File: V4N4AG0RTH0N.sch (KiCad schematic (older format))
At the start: 24 parts, among them SW1 SW_Push, U1 ATmega32U4-A, Y1 16MHz

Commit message: Almost done?
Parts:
- removed USB1: Molex-0548190589, random-keyboard-parts:Molex-0548190589, symbol random-keyboard-parts:Molex-0548190589
- added D10, D11, D12, D13, D14, D15, D16, D17, D18, D19, D20, D21, D22, D23, D24, D25, D26, D27, D28, D29, D3, D30, D31, D32, D33, D34, D35, D36, D37, D38, D39, D4, D40, D41, D42, D43, D44, D45, D46, D47, D48, D49, D5, D50, D6, D9: SOD-123, Diode_SMD:D_SOD-123, symbol Device:D_Small
- added D51, D52, D53: LED, LED_THT:LED_D3.0mm, symbol Device:LED
- added F2: Polyfuse_Small, Fuse:Fuse_1206_3216Metric, symbol Device:Polyfuse_Small
- added MX10, MX11, MX12, MX13, MX14, MX15, MX16, MX17, MX18, MX19, MX20, MX21, MX22, MX23, MX24, MX25, MX26, MX27, MX28, MX29, MX3, MX30, MX31, MX32, MX33, MX34, MX35, MX36, MX37, MX38, MX39, MX4, MX40, MX41, MX42, MX43, MX44, MX45, MX48, MX49, MX5, MX50, MX6, MX9: MX-NoLED, MX_Alps_Hybrid:MX-1U-NoLED, symbol MX_Alps_Hybrid:MX-NoLED
- added MX46, MX47: MX-NoLED, MX_Alps_Hybrid:MX-3U-ReversedStabilizers-NoLED, symbol MX_Alps_Hybrid:MX-NoLED
- added R5, R6, R7: 330, Resistor_SMD:R_0805_2012Metric, symbol Device:R_Small
- added R8, R9: 5.1K, Resistor_SMD:R_0805_2012Metric, symbol Device:R_Small
- added USB1: HRO-TYPE-C-31-M-12, Type-C:HRO-TYPE-C-31-M-12, symbol Type-C:HRO-TYPE-C-31-M-12
- F1: value 500mA -> Polyfuse_Small
- renumbered D3 to D2, D2 to D7, D4 to D8, MX3 to MX2, MX2 to MX7, MX4 to MX8
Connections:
- net labels added: COL10, COL11, COL2, COL3, COL4, COL5, COL6, COL7, COL8, COL9, LED_1, LED_2, LED_3, ROW2, ROW3, ROW4
- wire segments 58 -> 231
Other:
- moved on the sheet: D1, D2, D7, D8, MX1, MX2, MX7, MX8

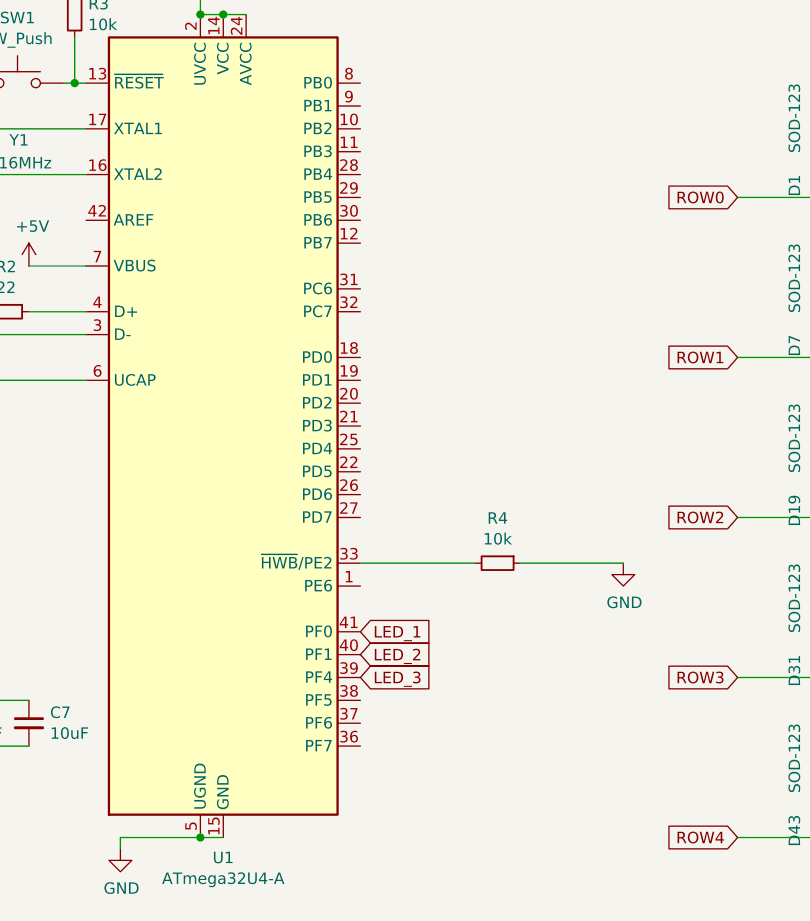
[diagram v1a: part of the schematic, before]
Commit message: Placed USB-C Components
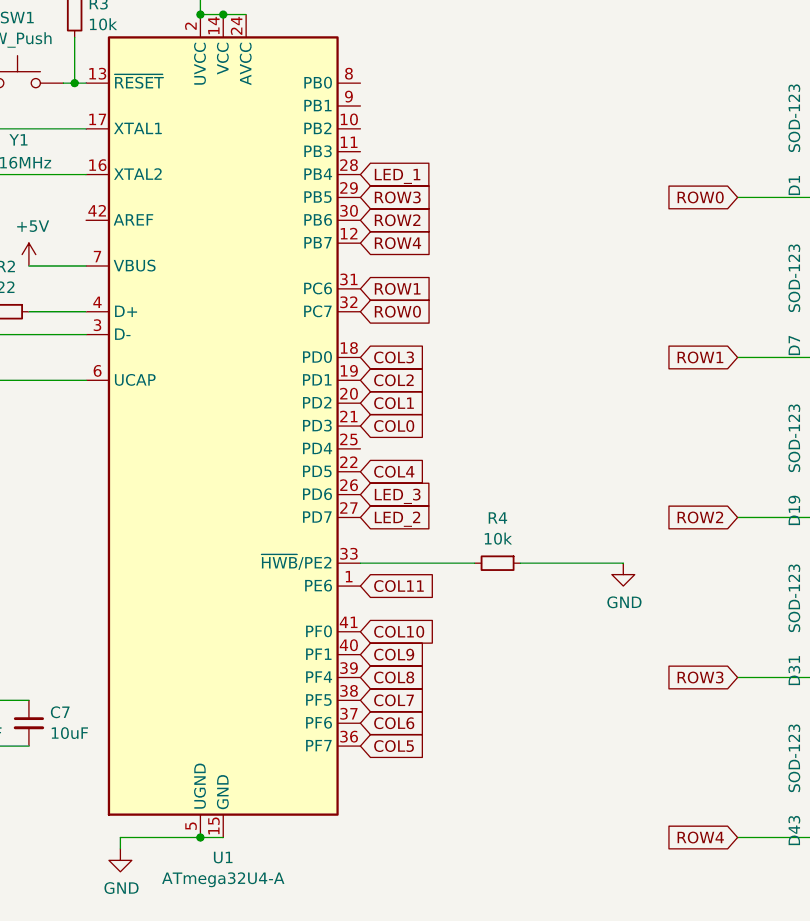
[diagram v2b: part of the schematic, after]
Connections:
- net COL0: now also U1.21 (PD3)
- net COL1: now also U1.20 (PD2)
- net COL10: now also U1.41 (PF0)
- net COL11: now also U1.1 (PE6)
- net COL2: now also U1.19 (PD1)
- net COL3: now also U1.18 (PD0)
- net COL4: now also U1.22 (PD5)
- net COL5: now also U1.36 (PF7)
- net COL6: now also U1.37 (PF6)
- net COL7: now also U1.38 (PF5)
- net COL8: now also U1.39 (PF4)
- net COL9: now also U1.40 (PF1)
- net LED_1: now also U1.28 (PB4); no longer U1.41 (PF0)
- net LED_2: now also U1.27 (PD7); no longer U1.40 (PF1)
- net LED_3: now also U1.26 (PD6); no longer U1.39 (PF4)
- net ROW0: now also U1.32 (PC7)
- net ROW1: now also U1.31 (PC6)
- net ROW2: now also U1.30 (PB6)
- net ROW3: now also U1.29 (PB5)
- net ROW4: now also U1.12 (PB7)
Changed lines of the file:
@@
 Wire Wire Line
 	1900 7050 2250 7050
-Text GLabel 3200 4400 2    50   Input ~ 0
+Text GLabel 3200 2400 2    50   Input ~ 0
 LED_1
-Text GLabel 3200 4500 2    50   Input ~ 0
+Text GLabel 3200 3900 2    50   Input ~ 0
 LED_2
-Text GLabel 3200 4600 2    50   Input ~ 0
+Text GLabel 3200 3800 2    50   Input ~ 0
 LED_3
 $Comp
@@
 	7050 7550 7050 7650
 Connection ~ 7050 7550
+Text GLabel 3200 2500 2    50   Input ~ 0
+ROW3
+Text GLabel 3200 2600 2    50   Input ~ 0
+ROW2
+Text GLabel 3200 2900 2    50   Input ~ 0
+ROW1
+Text GLabel 3200 3000 2    50   Input ~ 0
+ROW0
+Text GLabel 3200 2700 2    50   Input ~ 0
+ROW4
+Text GLabel 3200 3200 2    50   Input ~ 0
+COL3
+Text GLabel 3200 3300 2    50   Input ~ 0
+COL2
+Text GLabel 3200 3400 2    50   Input ~ 0
+COL1
+Text GLabel 3200 3500 2    50   Input ~ 0
+COL0
+Text GLabel 3200 3700 2    50   Input ~ 0
+COL4
+Text GLabel 3200 4900 2    50   Input ~ 0
+COL5
+Text GLabel 3200 4800 2    50   Input ~ 0
+COL6
+Text GLabel 3200 4700 2    50   Input ~ 0
+COL7
+Text GLabel 3200 4500 2    50   Input ~ 0
+COL9
+Text GLabel 3200 4400 2    50   Input ~ 0
+COL10
+Text GLabel 3200 4200 2    50   Input ~ 0
+COL11
+Text GLabel 3200 4600 2    50   Input ~ 0
+COL8
 $EndSCHEMATC
